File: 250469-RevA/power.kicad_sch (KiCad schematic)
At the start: 24 parts, among them J10 LED, J7 DIN-7, Q5 2SC1384, U21 4066, U22 7416, U3 74LS08

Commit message: Footprints and Symbols updates
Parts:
- CB1: footprint 250469-01:RockerSwitch_CuK_DPDT_E201J1AV2 -> 250469-01:Switch_DPDT_Power
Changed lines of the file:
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@@
       (effects (font (size 1.27 1.27)) hide)
     )
-    (property "Footprint" "250469-01:RockerSwitch_CuK_DPDT_E201J1AV2" (at 100.33 82.55 0)
+    (property "Footprint" "250469-01:Switch_DPDT_Power" (at 100.33 82.55 0)
       (effects (font (size 1.27 1.27)) hide)
     )

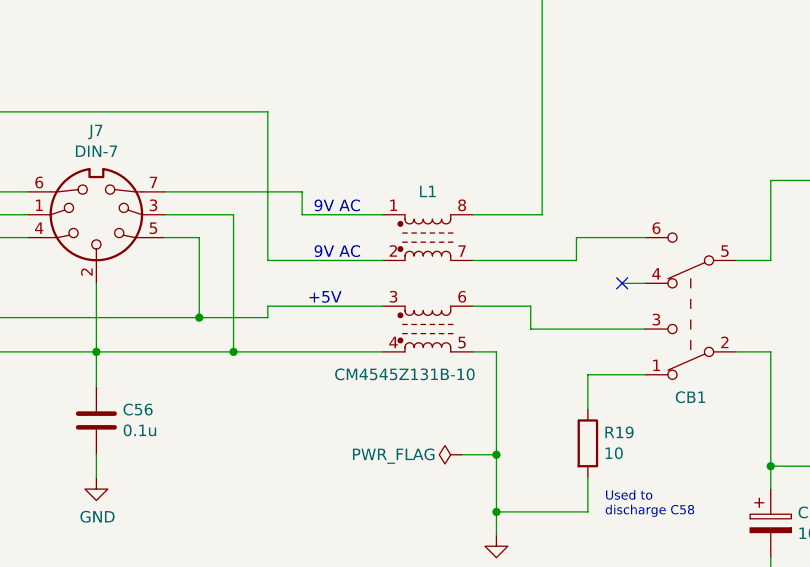
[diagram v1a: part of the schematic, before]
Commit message: Rename project library (not finished)
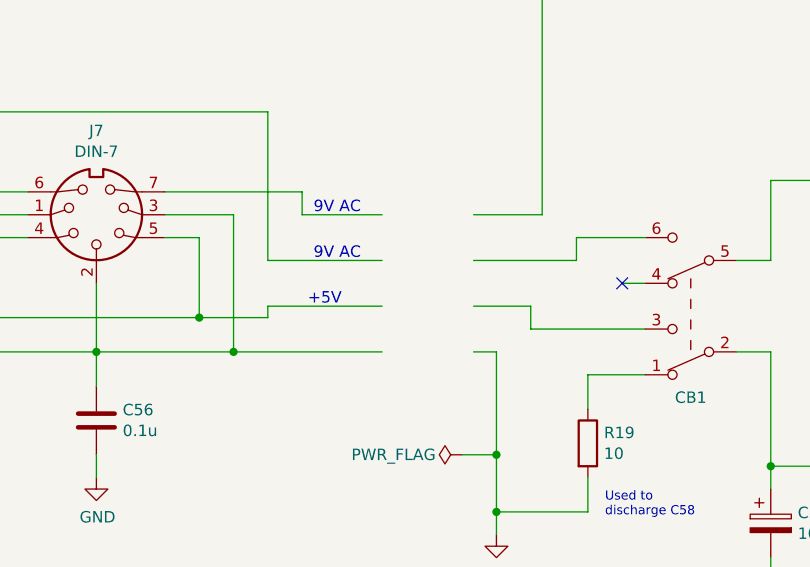
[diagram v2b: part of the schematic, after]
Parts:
- removed L1: CM4545Z131B-10, krl_Filter:Laird_CM4545Z131B-10, symbol krl_Filter:CM4545Z131B-10
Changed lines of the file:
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@@
-    )
-  )
-  (symbol (lib_id "krl_Filter:CM4545Z131B-10") (at 78.74 82.55 0) (unit 1)
-    (in_bom yes) (on_board yes) (dnp no)
-    (property "Reference" "L1" (at 78.74 72.39 0)
-      (effects (font (size 1.27 1.27)))
-    )
-    (property "Value" "CM4545Z131B-10" (at 76.2 92.71 0)
-      (effects (font (size 1.27 1.27)))
-    )
-    (property "Footprint" "krl_Filter:Laird_CM4545Z131B-10" (at 80.01 90.17 0)
-      (effects (font (size 1.27 1.27)) hide)
-    )
-    (property "Datasheet" "" (at 90.17 80.137 0)
-      (effects (font (size 1.27 1.27)) hide)
-    )
-    (pin "1")
-    (pin "2")
-    (pin "3")
-    (pin "4")
-    (pin "5")
-    (pin "6")
-    (pin "7")
-    (pin "8")
-    (instances
-      (project "C64C-250469-01-A"
-        (path "/ceb6c8ef-b249-4909-95e5-e7359667aee8/00000000-0000-0000-0000-00005e8458fd"
-          (reference "L1") (unit 1)
-        )
-      )
     )
   )

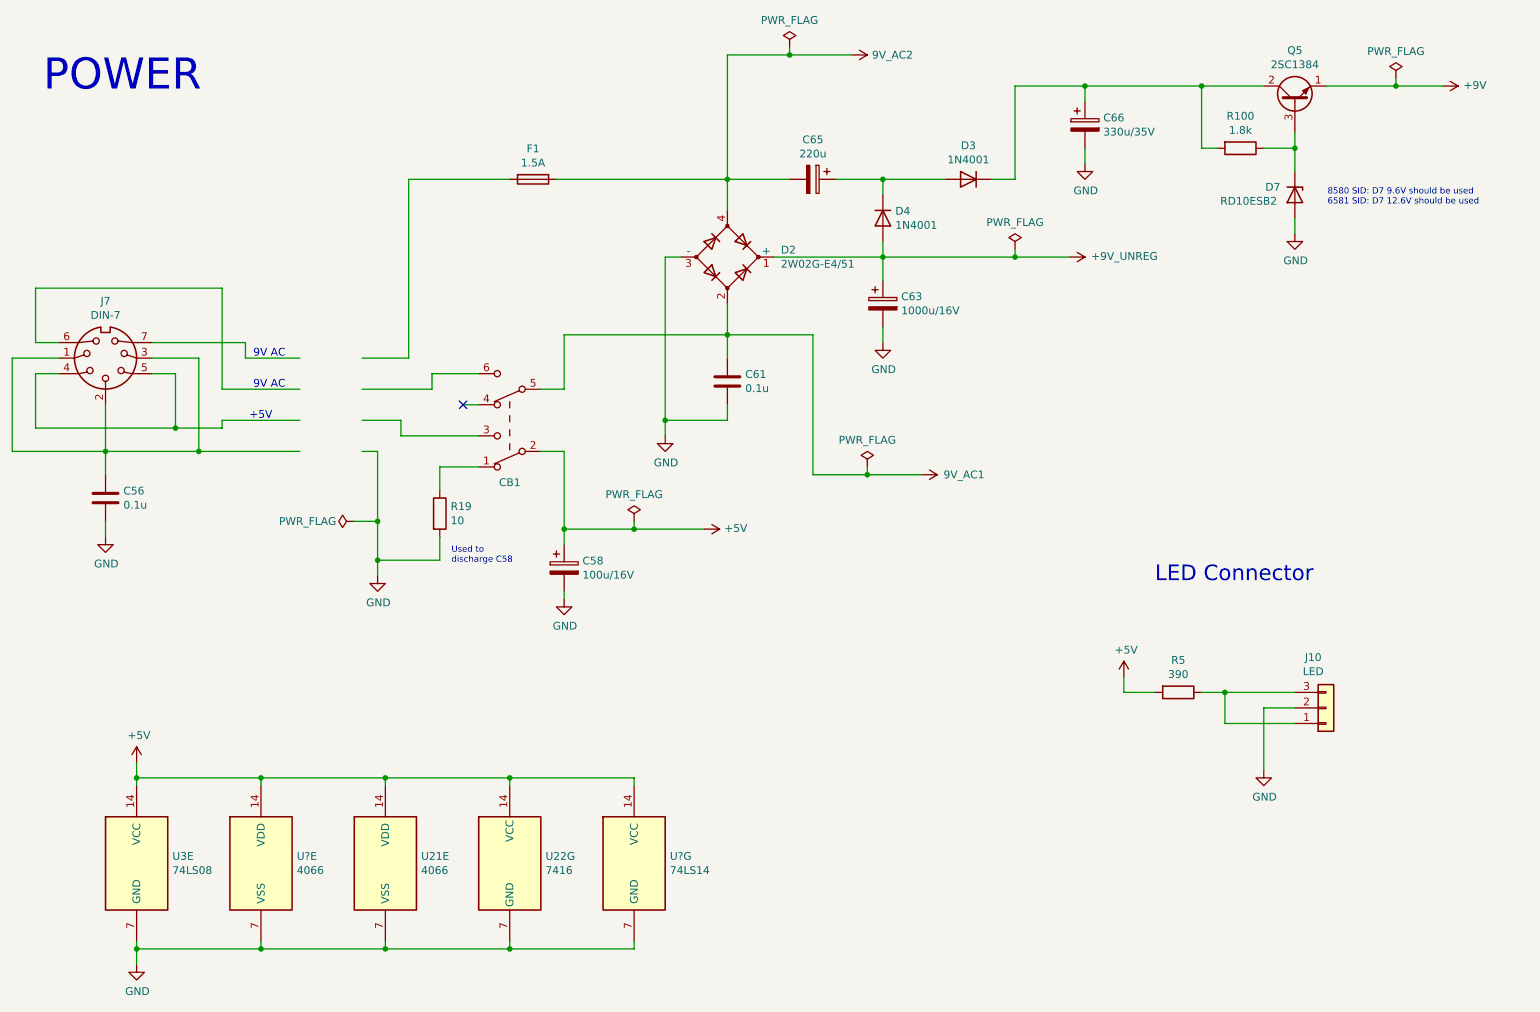
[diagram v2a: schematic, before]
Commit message: Fixes after renaming the project library
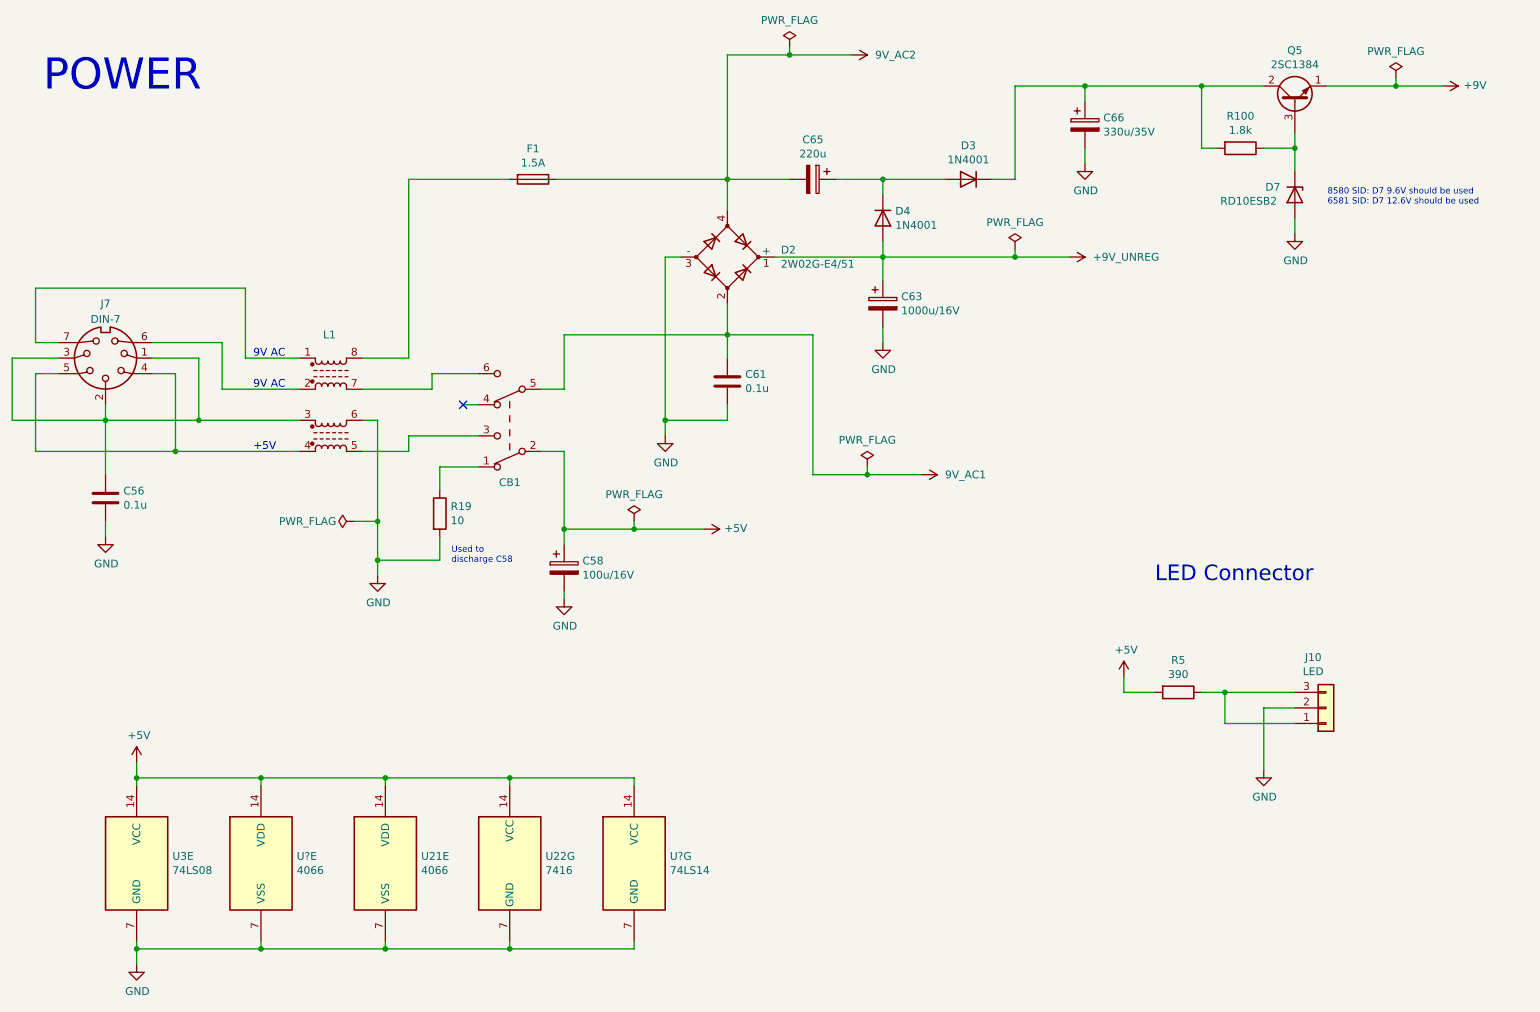
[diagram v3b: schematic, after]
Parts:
- added L1: Filter_CommonModeChoke_Dual, C64-C-250469:Filter_CommonModeChoke_Dual, symbol C64-C-250469:Filter_CommonModeChoke_Dual
- CB1: footprint 250469-01:Switch_DPDT_Power -> C64-C-250469:Switch_DPDT_Power
- F1: footprint 250469-01:Fuseclip_Cylinder-6.3x32mm -> C64-C-250469:Fuseclip_Cylinder-6.3x32mm
- J7: footprint krl_Connector_DIN:C64_Original_DIN-7_Circular -> C64-C-250469:Connector_DIN-7_Power
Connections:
- net GND: now also L1.6
- net at C56.1, J7.1, J7.2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: now also L1.3
- net at J7.4, J7.5: now also L1.4
- net at J7.6: now also L1.2
- net at J7.7: now also L1.1
- net at F1.2: now also L1.8
- net at CB1.3 (C): now also L1.5
- net at CB1.6 (C): now also L1.7
